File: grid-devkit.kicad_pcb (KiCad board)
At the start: 4 copper layers, 39 x 107.3 mm, 168 parts, among them J601 TYPE-C-32-M-12, J603 Conn_01x04, J604 Conn_01x04, J610 Conn_01x08, J611 Conn_01x08, J701 C5137195, J702 Conn_02x05_Odd_Even, SW609 model_code, SW610 rev_code, SW701 C255807, SW702 C2905169, SW703 C2905169, U1001 74HC4051, U1002 74HC4051, U601 LN1134A332MR-G, U602 C5451661, U603 C5451661, U604 74LVC1G08, U605 BL1551B, U606 BL1551B, U607 BL1551B, U608 BL1551B, U609 74HC165, U610 APS1604M-3SQR-ZR, U703 RP2040, U704 ESP32-S3, U705 W25Q64JVSSIQ, U801 74HC165, U903 APS1604M-3SQR-SN, U918 NS4168_C910588, Y701 40MHz

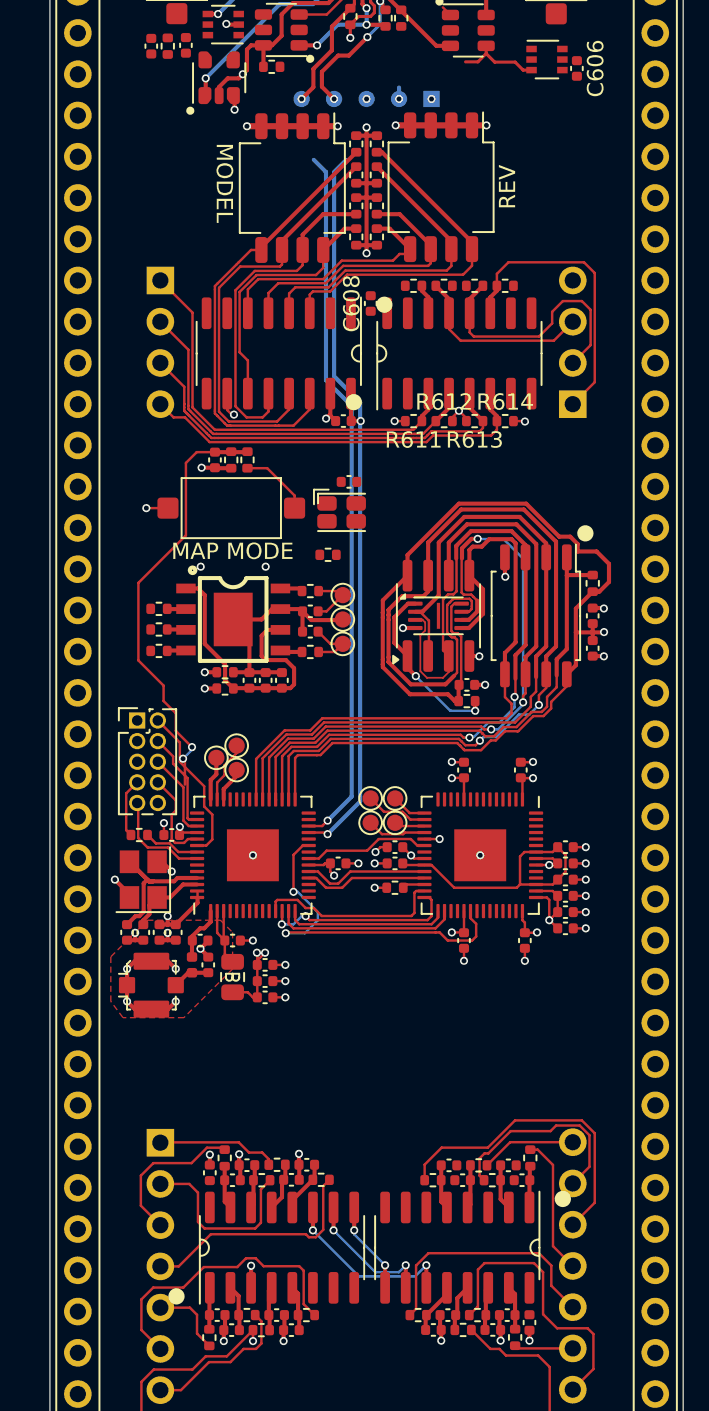
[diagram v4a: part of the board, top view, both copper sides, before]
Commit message: SUKU memory layout optimized
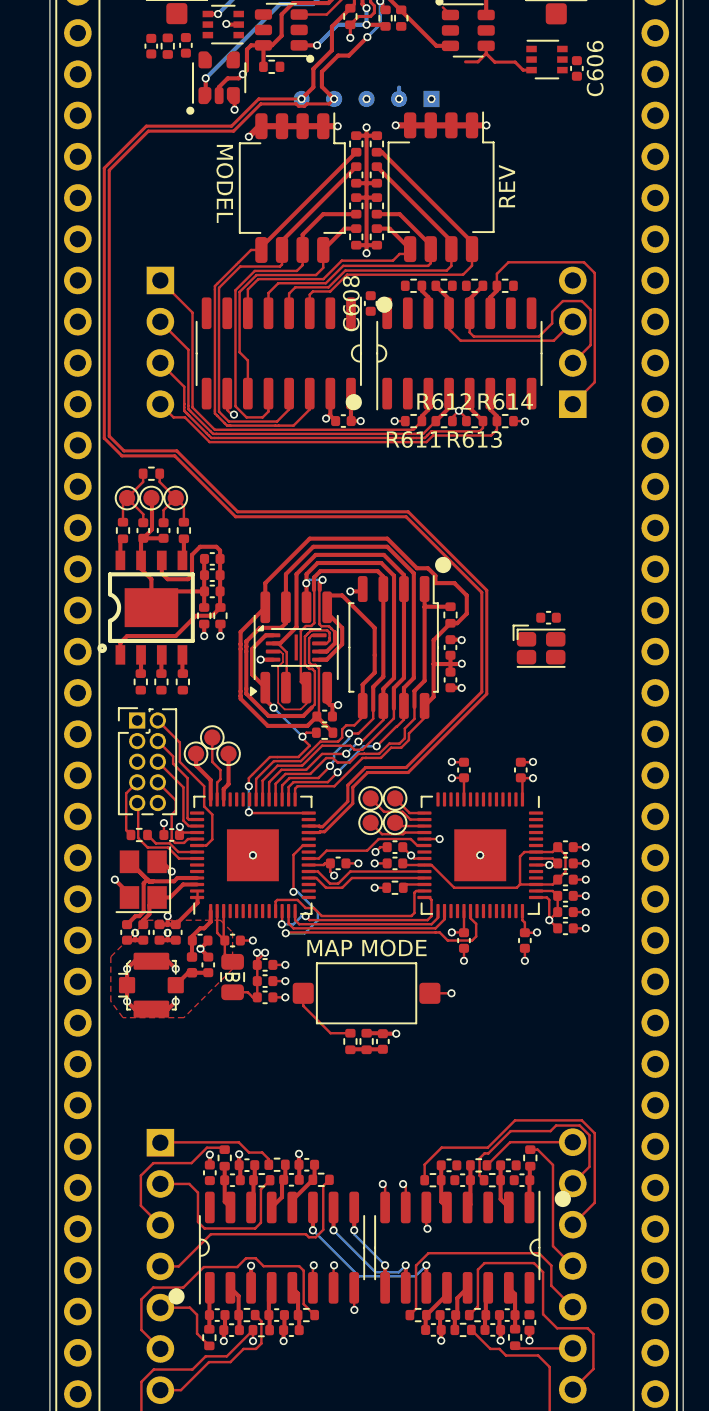
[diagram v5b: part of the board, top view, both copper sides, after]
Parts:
- moved C757 37.3 mm to (101.0, 121.5), turned to 90 degrees
- moved R701 36.8 mm to (100.0, 121.5), turned to -90 degrees
- moved R736 36.4 mm to (99.0, 121.5), turned to -90 degrees
- moved SW701 31.0 mm to (100.0, 118.5), turned to 0 degrees
- moved C901 14.9 mm to (111.2, 95.4)
- moved D901 14.9 mm to (110.8, 97.2)
- moved TP901 14.6 mm to (85.2, 88.0), turned to -90 degrees
- moved TP903 14.0 mm to (86.7, 88.0), turned to -90 degrees
- moved TP902 13.7 mm to (88.2, 88.0), turned to -90 degrees
- moved L902 12.1 mm to (85.0, 90.0), turned to -90 degrees
- moved R606 12.0 mm to (86.7, 86.5)
- moved C940 11.4 mm to (86.2, 90.0), turned to -90 degrees
- moved C939 11.0 mm to (87.5, 90.0), turned to -90 degrees
- moved L903 10.8 mm to (88.7, 90.0), turned to 90 degrees
- moved U705 8.97 mm to (101.7, 97.2)
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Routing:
- net /MCU/USB_DN: track 59.7 -> 96.0 mm, vias 4 -> 3
- net /MCU/USB_DP: track 52.0 -> 87.0 mm, vias 2 -> 1
- net /MCU/MAP_MODE: track 26.7 -> 1.97 mm, vias 2 -> 0
- net /MCU/SPICLK: track 57.7 -> 34.1 mm, vias 3 -> 4
- net /MCU/SPID: track 39.5 -> 24.3 mm
- net /MCU/SPIHD: track 61.5 -> 49.8 mm
- net /MCU/SPIWP: track 47.9 -> 36.5 mm
- net /MCU/SPIQ: track 47.1 -> 36.1 mm
- net /MCU/SPICS0: track 32.2 -> 21.6 mm
- net VDD_SPI: track 68.9 -> 58.3 mm, vias 2 -> 1
- net GND: track 70.6 -> 80.2 mm, vias 59 -> 63
- net /MCU/SPICS1: track 10.9 -> 20.4 mm, vias 2 -> 4
- net Net-(C939-Pad1): track 3.53 -> 5.44 mm
- net Net-(C940-Pad1): track 3.53 -> 5.44 mm
- net ESP_GPIO_35: track 2.15 -> 2.94 mm

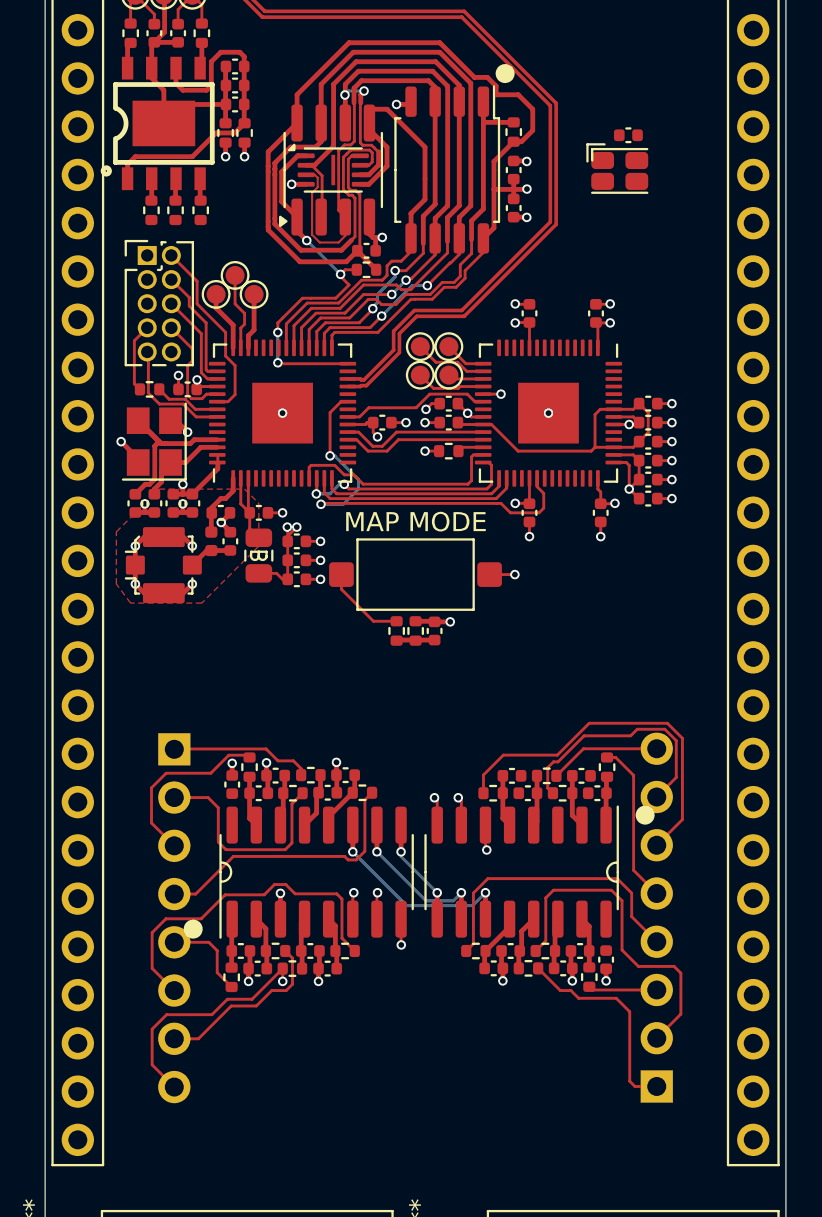
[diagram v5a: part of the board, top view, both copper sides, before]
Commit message: SUKU analog layout grid alignment fixed, mcu connection routed
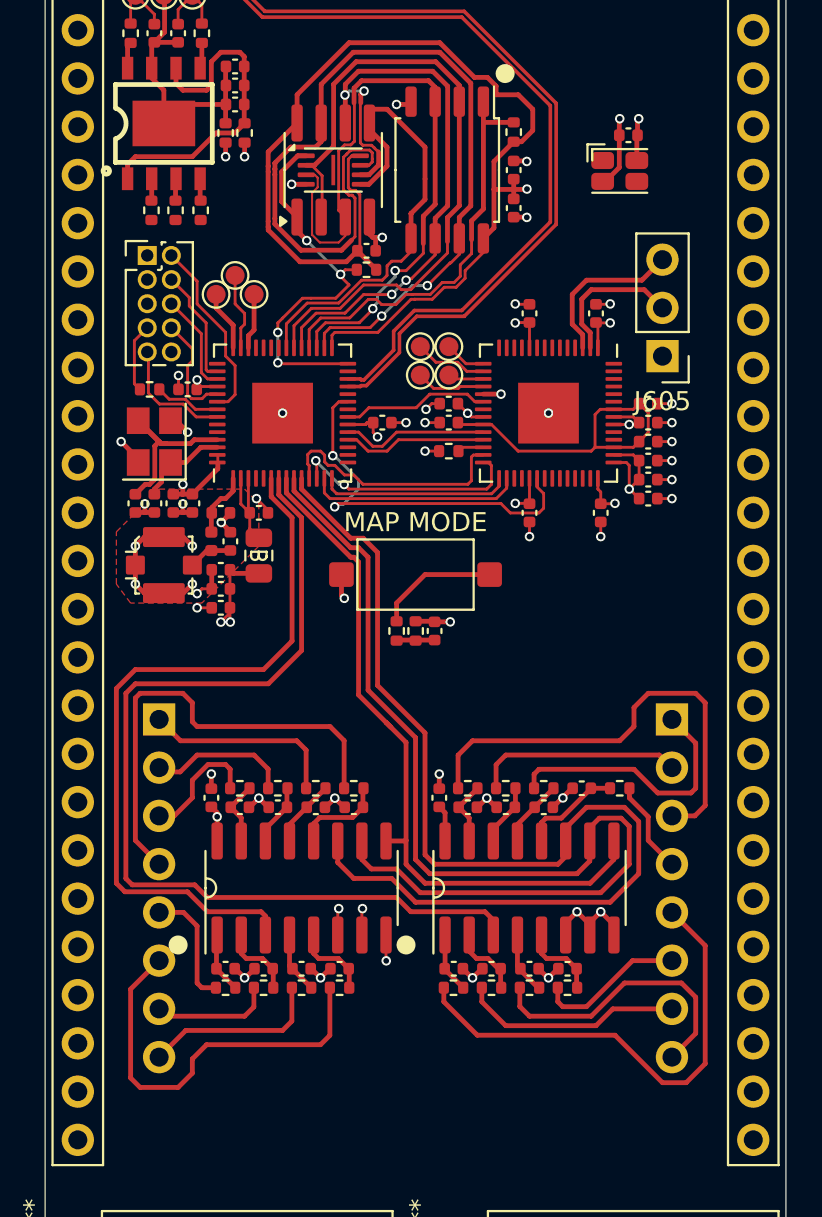
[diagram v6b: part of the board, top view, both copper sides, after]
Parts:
- added J605: Conn_01x03, Connector_PinHeader_2.54mm:PinHeader_1x03_P2.54mm_Vertical, F.Cu at (113.0, 107.0)
- moved J611 19.3 mm to (113.5, 126.1), turned to 180 degrees
- moved R1011 14.1 mm to (102.0, 140.2), turned to 180 degrees
- moved C1018 12.2 mm to (101.2, 130.2), turned to 90 degrees
- moved C1012 11.9 mm to (102.0, 139.2), turned to 0 degrees
- moved R1010 11.8 mm to (102.8, 129.8), turned to 180 degrees
- moved R1014 11.4 mm to (110.8, 129.8), turned to 0 degrees
- moved C1013 11.2 mm to (104.0, 139.2), turned to 180 degrees
- moved R1016 11.2 mm to (106.0, 140.2), turned to 180 degrees
- moved R1015 11.0 mm to (108.0, 140.2)
- moved R1012 10.9 mm to (104.0, 140.2)
- moved C1016 10.6 mm to (108.0, 139.2), turned to 180 degrees
- moved C1015 10.6 mm to (108.8, 129.8), turned to 180 degrees
- moved C1011 9.60 mm to (102.8, 130.8), turned to 0 degrees
- moved R1009 9.52 mm to (106.8, 129.8), turned to 180 degrees
- moved C1017 9.24 mm to (106.0, 139.2), turned to 0 degrees
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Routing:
- net ESP_GPIO_2: track 0.00 -> 50.5 mm
- net ESP_GPIO_5: track 11.2 -> 58.4 mm, vias 2 -> 0
- net ESP_GPIO_4: track 8.49 -> 55.3 mm, vias 2 -> 0
- net ESP_GPIO_1: track 1.36 -> 39.1 mm, vias 1 -> 0
- net ESP_GPIO_3: track 5.74 -> 37.3 mm, vias 2 -> 0
- net /ANA_6: track 3.62 -> 24.3 mm
- net /ANA_10: track 8.51 -> 25.4 mm
- net /ANA_11: track 19.1 -> 7.86 mm
- net /sheet5D8763D6/IN_3: track 15.3 -> 4.92 mm
- net /Sheet5D7C8BFD/IN_3: track 14.4 -> 24.5 mm
- net /ANA_15: track 5.87 -> 15.2 mm
- net /MCU/RP_UART0_RX: track 0.00 -> 8.55 mm
- net GND: track 80.2 -> 88.4 mm, vias 63 -> 64
- net /MCU/RP_UART0_TX: track 0.00 -> 7.60 mm
- net /ANA_3: track 17.6 -> 11.0 mm
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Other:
- board text added: "4051 POSITION (x = 94, y = 135) 4051 POSITION (x = 106, y = 135) GRID = 0.25mm"

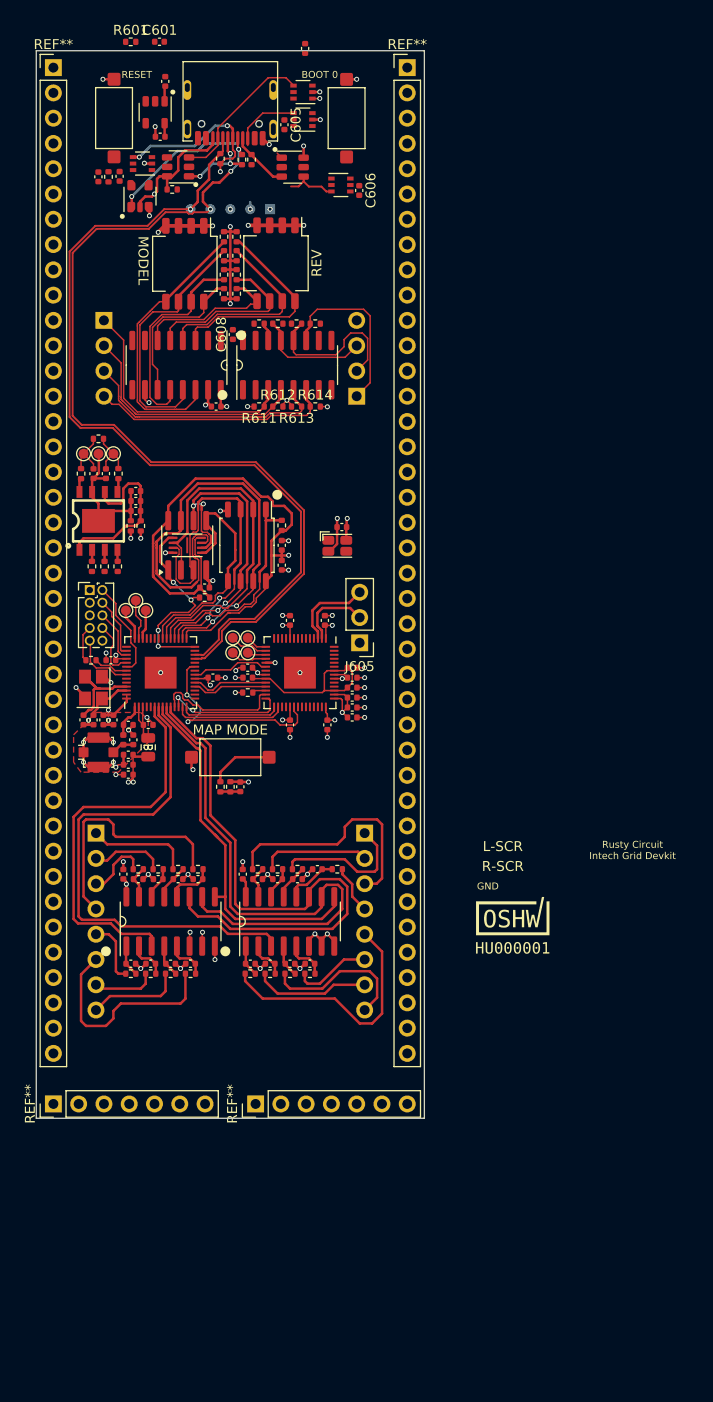
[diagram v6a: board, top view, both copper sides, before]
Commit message: Removes unused refs, adjusts size, and adds traces for LED, boot, and reset
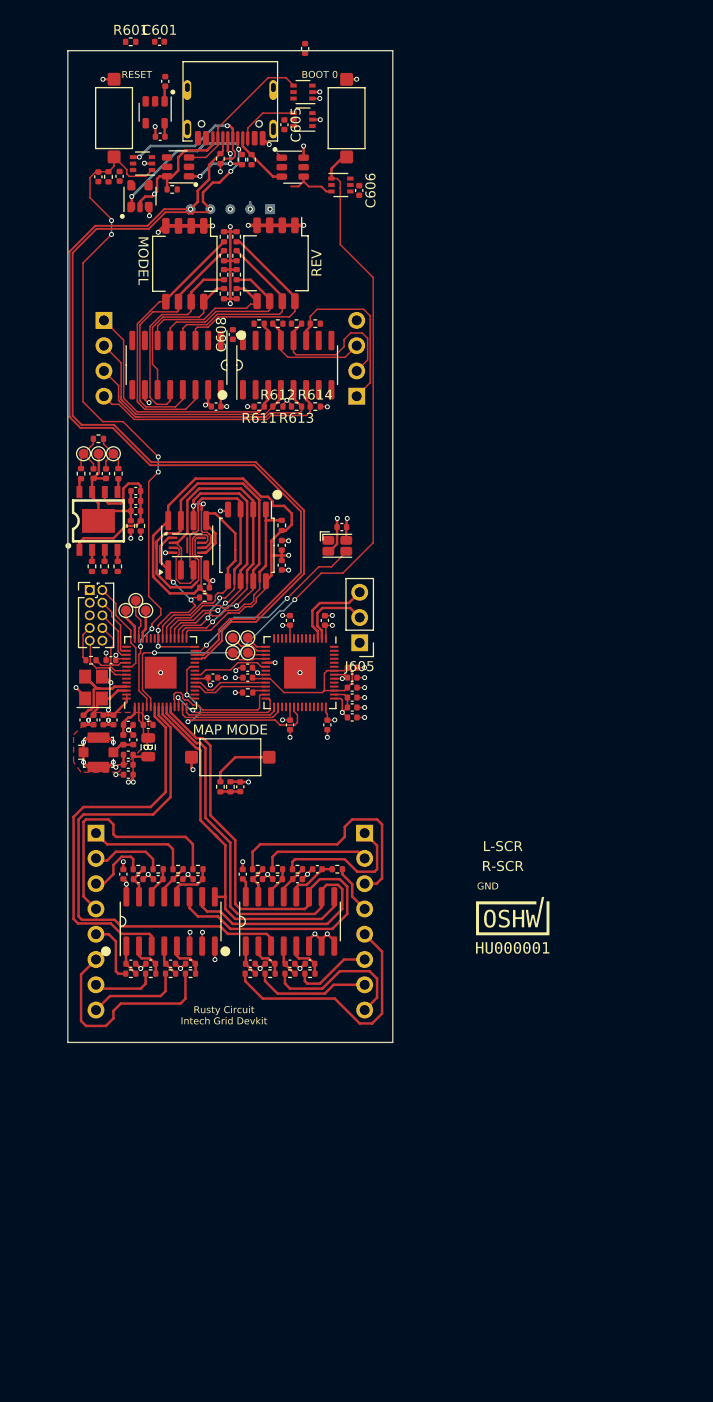
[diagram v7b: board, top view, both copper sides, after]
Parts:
- removed REF** (x2): PinHeader_1x07_P2.54mm_Vertical, Connector_PinHeader_2.54mm:PinHeader_1x07_P2.54mm_Vertical
- removed REF** (x2): PinHeader_1x40_P2.54mm_Vertical, Connector_PinHeader_2.54mm:PinHeader_1x40_P2.54mm_Vertical
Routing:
- net /MCU/ESP_BOOT0: track 0.00 -> 75.1 mm, vias 0 -> 2
- net /MCU/ESP_RESET: track 0.00 -> 70.7 mm, vias 0 -> 6
- net /MCU/LED_DATA_OUT: track 0.00 -> 19.4 mm, vias 0 -> 2
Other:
- board size 39 x 107.3 mm -> 32.7 x 99.7 mm

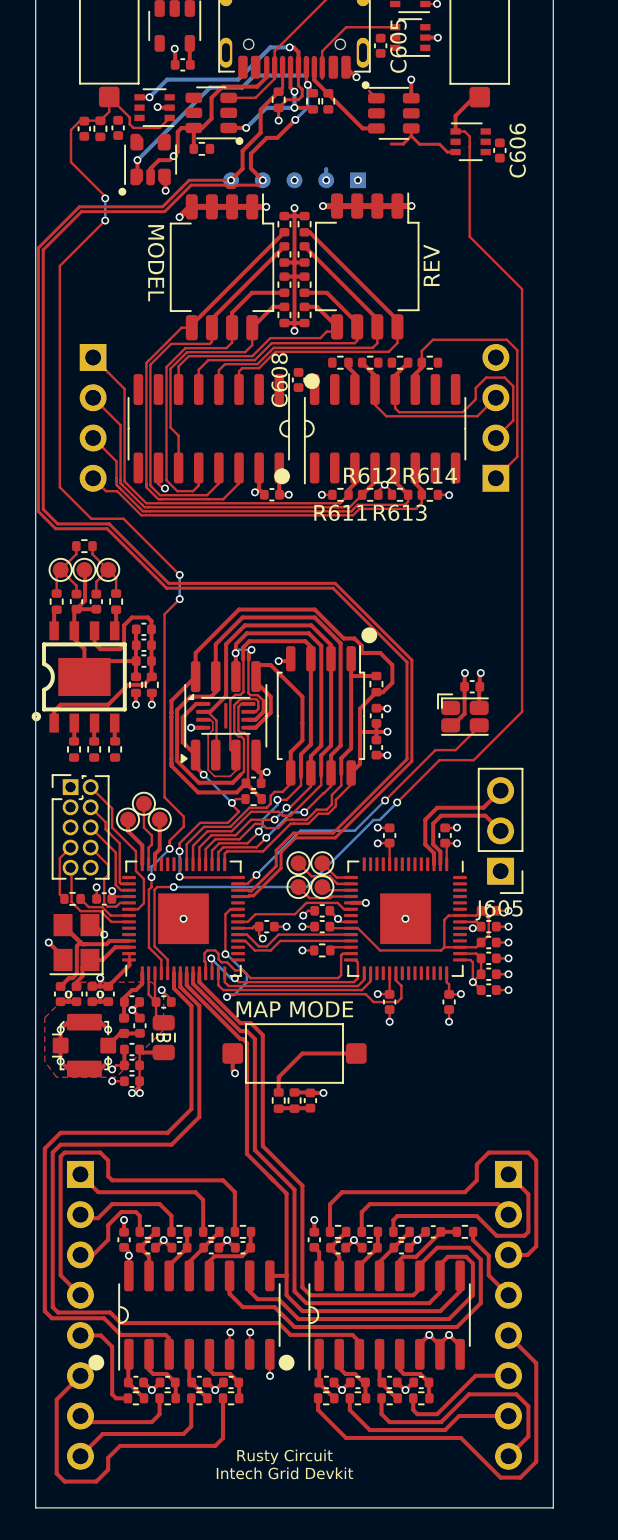
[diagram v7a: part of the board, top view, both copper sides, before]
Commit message: Adds traces for shift registers
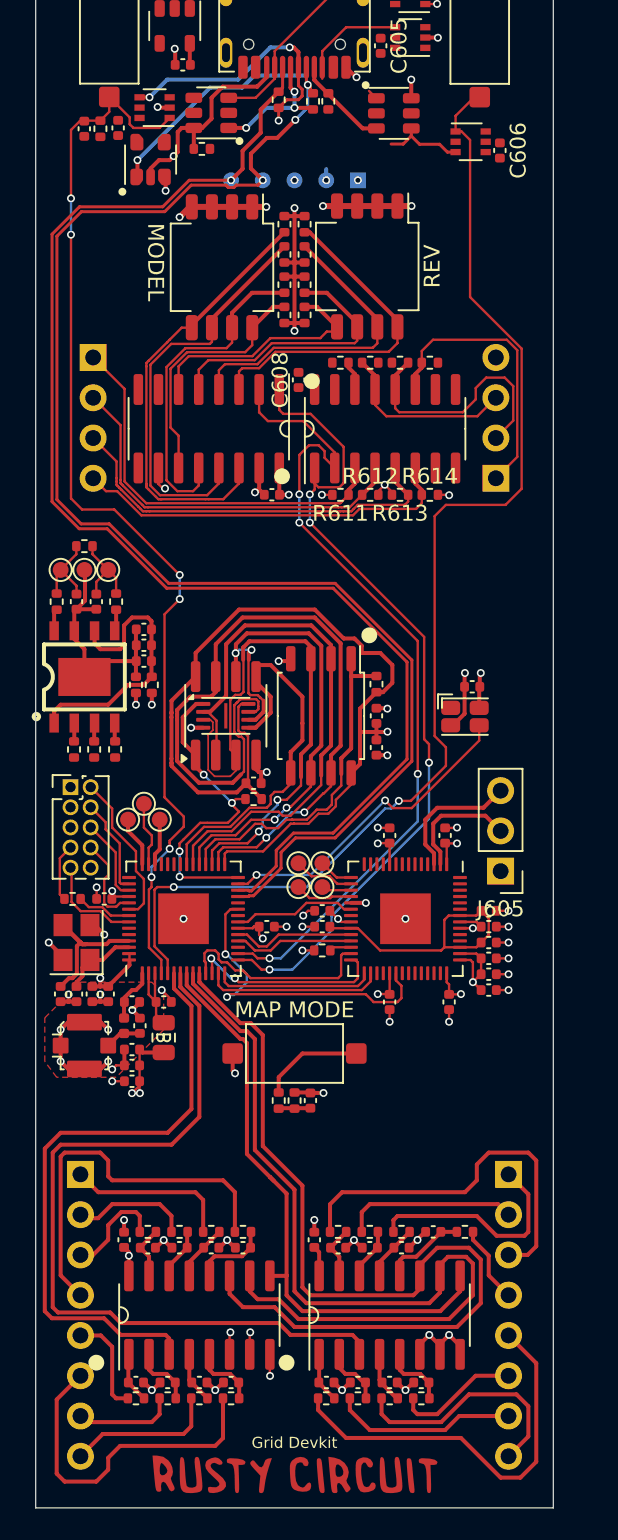
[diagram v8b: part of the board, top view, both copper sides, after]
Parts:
- added G*** (x2): LOGO, LOGO, F.Cu at (100.0, 145.1)
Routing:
- net /LCDBUTTON/SHIFT: track 0.00 -> 53.8 mm, vias 0 -> 4
- net /LCDBUTTON/CLOCK: track 0.00 -> 52.9 mm, vias 0 -> 4
- net /MCU/ESP_RESET: track 70.7 -> 68.3 mm
- net /MCU/ESP_BOOT0: track 75.1 -> 76.9 mm
- net /MCU/USB_DP: track 87.0 -> 85.5 mm
- net /MCU/USB_DN: track 96.0 -> 94.4 mm
- net /MCU/LED_DATA_OUT: track 19.4 -> 20.3 mm
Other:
- board text added: "Grid Devkit"
- board text removed: "Rusty Circuit Intech Grid Devkit"
